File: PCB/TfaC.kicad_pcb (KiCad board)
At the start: 2 copper layers, 105 x 54 mm, 52 parts, among them IC501 ATMEGA88-A, M301 DisplayModule, P101 Line, P501 PRG, Q401 IRLML2502, Q402 IRLML2502, Q403 IRLML2502, Q404 IRLML2502, Q405 IRLML2502, Q406 IRLML2502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

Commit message: Touched up some routs to avoid zone borders
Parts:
- moved G*** 7.87 mm to (180.2, 68.1)
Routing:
- net /Controller/~RTC_SELECT: track 80.3 -> 119.6 mm
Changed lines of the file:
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@@
     (thickness 1.6)
     (drawings 64)
-    (tracks 431)
+    (tracks 435)
     (zones 0)
     (modules 52)
@@
   )
   (setup
-    (last_trace_width 0.1524)
+    (last_trace_width 0.3048)
     (user_trace_width 0.3048)
     (user_trace_width 0.6096)
@@
   )
   (module tfac-footprints:sm-logo-1200 (layer F.Cu)
-    (at 188.087 68.072)
+    (at 180.213 68.072)
     (fp_text reference G*** (at 0 0) (layer F.SilkS) hide
       (effects (font (thickness 0.3)))
@@
   (segment (start 148.148 85.41) (end 148.148 87.242) (width 0.6096) (layer F.Cu) (net 15))
   (segment (start 147.24 84.502) (end 148.148 85.41) (width 0.6096) (layer F.Cu) (net 15))
-  (segment (start 136.38022 101.092) (end 136.38022 98.69678) (width 0.3048) (layer F.Cu) (net 16))
-  (segment (start 181.362 83.306) (end 181.362 82.618) (width 0.3048) (layer F.Cu) (net 16))
-  (segment (start 180.721 83.947) (end 181.362 83.306) (width 0.3048) (layer F.Cu) (net 16))
-  (segment (start 180.721 84.201) (end 180.721 83.947) (width 0.3048) (layer F.Cu) (net 16))
-  (segment (start 180.594 84.328) (end 180.721 84.201) (width 0.3048) (layer F.Cu) (net 16))
-  (via (at 180.594 84.328) (size 0.6858) (drill 0.3302) (layers F.Cu B.Cu) (net 16))
-  (segment (start 179.324 85.598) (end 180.594 84.328) (width 0.3048) (layer B.Cu) (net 16))
-  (segment (start 170.561 85.598) (end 179.324 85.598) (width 0.3048) (layer B.Cu) (net 16))
-  (segment (start 159.131 97.028) (end 170.561 85.598) (width 0.3048) (layer B.Cu) (net 16))
-  (segment (start 140.335 97.028) (end 159.131 97.028) (width 0.3048) (layer B.Cu) (net 16))
-  (segment (start 140.081 96.774) (end 140.335 97.028) (width 0.3048) (layer B.Cu) (net 16))
-  (via (at 140.081 96.774) (size 0.6858) (drill 0.3302) (layers F.Cu B.Cu) (net 16))
-  (segment (start 138.303 96.774) (end 140.081 96.774) (width 0.3048) (layer F.Cu) (net 16))
-  (segment (start 136.38022 98.69678) (end 138.303 96.774) (width 0.3048) (layer F.Cu) (net 16))
+  (segment (start 138.684 102.188) (end 138.684 103.759) (width 0.3048) (layer F.Cu) (net 16) (status 400000))
+  (segment (start 180.721 83.82) (end 181.362 83.179) (width 0.3048) (layer F.Cu) (net 16) (status 800000))
+  (segment (start 180.721 84.201) (end 180.721 83.82) (width 0.3048) (layer F.Cu) (net 16))
+  (segment (start 180.34 84.582) (end 180.721 84.201) (width 0.3048) (layer F.Cu) (net 16))
+  (via (at 180.34 84.582) (size 0.6858) (drill 0.3302) (layers F.Cu B.Cu) (net 16))
+  (segment (start 179.705 85.217) (end 180.34 84.582) (width 0.3048) (layer B.Cu) (net 16))
+  (segment (start 173.355 85.217) (end 179.705 85.217) (width 0.3048) (layer B.Cu) (net 16))
+  (segment (start 153.543 105.029) (end 173.355 85.217) (width 0.3048) (layer B.Cu) (net 16))
+  (segment (start 139.954 105.029) (end 153.543 105.029) (width 0.3048) (layer B.Cu) (net 16))
+  (segment (start 139.827 104.902) (end 139.954 105.029) (width 0.3048) (layer B.Cu) (net 16))
+  (via (at 139.827 104.902) (size 0.6858) (drill 0.3302) (layers F.Cu B.Cu) (net 16))
+  (segment (start 138.684 103.759) (end 139.827 104.902) (width 0.3048) (layer F.Cu) (net 16))
+  (segment (start 181.362 83.179) (end 181.362 82.618) (width 0.3048) (layer F.Cu) (net 16) (status C00000))
   (segment (start 136.38022 101.092) (end 137.588 101.092) (width 0.6096) (layer F.Cu) (net 16))
   (segment (start 137.588 101.092) (end 138.684 102.188) (width 0.6096) (layer F.Cu) (net 16))
@@
   (segment (start 136.38022 86.36) (end 137.588 86.36) (width 0.6096) (layer F.Cu) (net 17))
   (segment (start 137.588 86.36) (end 138.938 87.71) (width 0.6096) (layer F.Cu) (net 17))
+  (segment (start 119.634 86.741) (end 119.634 102.108) (width 0.3048) (layer B.Cu) (net 18))
   (segment (start 117.87378 79.0448) (end 117.87378 81.55178) (width 0.3048) (layer F.Cu) (net 18))
+  (segment (start 119.634 83.312) (end 119.634 86.741) (width 0.3048) (layer B.Cu) (net 18))
+  (segment (start 118.618 82.296) (end 119.634 83.312) (width 0.3048) (layer B.Cu) (net 18))
+  (via (at 118.618 82.296) (size 0.6858) (drill 0.3302) (layers F.Cu B.Cu) (net 18))
+  (segment (start 117.87378 81.55178) (end 118.618 82.296) (width 0.3048) (layer F.Cu) (net 18))
+  (segment (start 171.196 101.854) (end 175.514 97.536) (width 0.3048) (layer B.Cu) (net 18))
+  (segment (start 171.196 108.331) (end 171.196 101.854) (width 0.3048) (layer B.Cu) (net 18))
+  (segment (start 162.306 117.221) (end 171.196 108.331) (width 0.3048) (layer B.Cu) (net 18))
+  (segment (start 120.65 117.221) (end 162.306 117.221) (width 0.3048) (layer B.Cu) (net 18))
+  (segment (start 117.856 114.427) (end 120.65 117.221) (width 0.3048) (layer B.Cu) (net 18))
+  (segment (start 117.856 103.886) (end 117.856 114.427) (width 0.3048) (layer B.Cu) (net 18))
+  (segment (start 119.634 102.108) (end 117.856 103.886) (width 0.3048) (layer B.Cu) (net 18))
+  (segment (start 174.752 98.298) (end 175.514 97.536) (width 0.3048) (layer B.Cu) (net 18))
   (segment (start 178.962 92.564) (end 178.962 91.118) (width 0.3048) (layer F.Cu) (net 18))
   (segment (start 178.943 92.583) (end 178.962 92.564) (width 0.3048) (layer F.Cu) (net 18))
   (via (at 178.943 92.583) (size 0.6858) (drill 0.3302) (layers F.Cu B.Cu) (net 18))
   (segment (start 178.943 94.107) (end 178.943 92.583) (width 0.3048) (layer B.Cu) (net 18))
-  (segment (start 174.752 98.298) (end 178.943 94.107) (width 0.3048) (layer B.Cu) (net 18))
-  (segment (start 167.64 98.298) (end 174.752 98.298) (width 0.3048) (layer B.Cu) (net 18))
-  (segment (start 167.005 97.663) (end 167.64 98.298) (width 0.3048) (layer B.Cu) (net 18))
-  (segment (start 130.556 97.663) (end 167.005 97.663) (width 0.3048) (layer B.Cu) (net 18))
-  (segment (start 119.634 86.741) (end 130.556 97.663) (width 0.3048) (layer B.Cu) (net 18))
-  (segment (start 119.634 83.312) (end 119.634 86.741) (width 0.3048) (layer B.Cu) (net 18))
-  (segment (start 118.618 82.296) (end 119.634 83.312) (width 0.3048) (layer B.Cu) (net 18))
-  (via (at 118.618 82.296) (size 0.6858) (drill 0.3302) (layers F.Cu B.Cu) (net 18))
-  (segment (start 117.87378 81.55178) (end 118.618 82.296) (width 0.3048) (layer F.Cu) (net 18))
+  (segment (start 175.514 97.536) (end 178.943 94.107) (width 0.3048) (layer B.Cu) (net 18))
   (segment (start 115.4176 77.644) (end 116.47298 77.644) (width 0.6096) (layer F.Cu) (net 18))
   (segment (start 116.47298 77.644) (end 117.87378 79.0448) (width 0.6096) (layer F.Cu) (net 18))

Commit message: Created gerbers for TfaC-Rev 2L.2.a2f0245
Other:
- board text added: "TfaC Rev 2L.2.a2f0245"
- board text removed: "TfaC Rev 2L.2"
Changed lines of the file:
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@@
   )
   (setup
-    (last_trace_width 0.3048)
+    (last_trace_width 0.1524)
     (user_trace_width 0.3048)
     (user_trace_width 0.6096)
@@
     (effects (font (size 0.762 0.762) (thickness 0.127)))
   )
-  (gr_text "TfaC\nRev 2L.2\n" (at 200.5584 68.3768) (layer F.SilkS)
+  (gr_text "TfaC\nRev 2L.2.a2f0245\n" (at 200.5584 68.3768) (layer F.SilkS)
     (effects (font (size 1.27 1.27) (thickness 0.127)) (justify right))
   )
@@
   (segment (start 148.148 85.41) (end 148.148 87.242) (width 0.6096) (layer F.Cu) (net 15))
   (segment (start 147.24 84.502) (end 148.148 85.41) (width 0.6096) (layer F.Cu) (net 15))
-  (segment (start 138.684 102.188) (end 138.684 103.759) (width 0.3048) (layer F.Cu) (net 16) (status 400000))
-  (segment (start 180.721 83.82) (end 181.362 83.179) (width 0.3048) (layer F.Cu) (net 16) (status 800000))
+  (segment (start 138.684 102.188) (end 138.684 103.759) (width 0.3048) (layer F.Cu) (net 16))
+  (segment (start 180.721 83.82) (end 181.362 83.179) (width 0.3048) (layer F.Cu) (net 16))
   (segment (start 180.721 84.201) (end 180.721 83.82) (width 0.3048) (layer F.Cu) (net 16))
   (segment (start 180.34 84.582) (end 180.721 84.201) (width 0.3048) (layer F.Cu) (net 16))
@@
   (via (at 139.827 104.902) (size 0.6858) (drill 0.3302) (layers F.Cu B.Cu) (net 16))
   (segment (start 138.684 103.759) (end 139.827 104.902) (width 0.3048) (layer F.Cu) (net 16))
-  (segment (start 181.362 83.179) (end 181.362 82.618) (width 0.3048) (layer F.Cu) (net 16) (status C00000))
+  (segment (start 181.362 83.179) (end 181.362 82.618) (width 0.3048) (layer F.Cu) (net 16))
   (segment (start 136.38022 101.092) (end 137.588 101.092) (width 0.6096) (layer F.Cu) (net 16))
   (segment (start 137.588 101.092) (end 138.684 102.188) (width 0.6096) (layer F.Cu) (net 16))

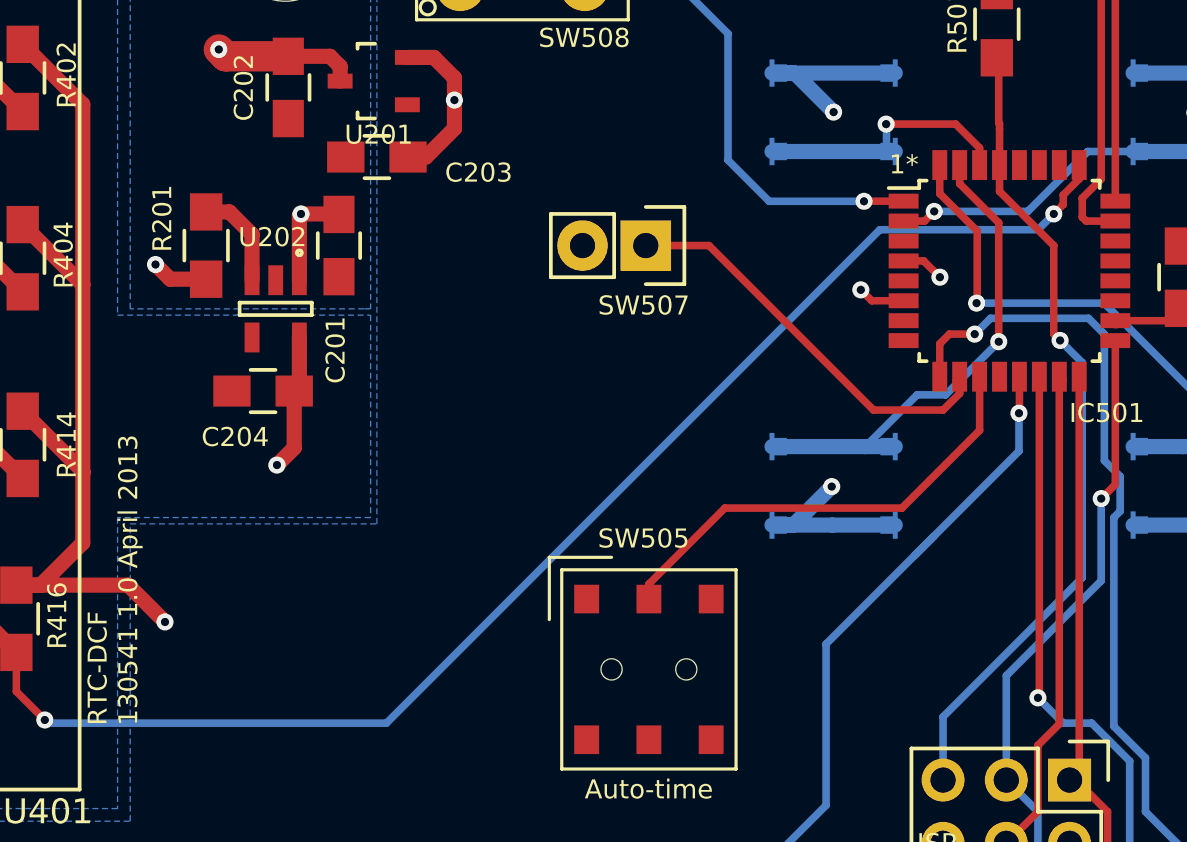
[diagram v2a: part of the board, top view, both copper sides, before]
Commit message: Added indicator LEDs and Heartbeat
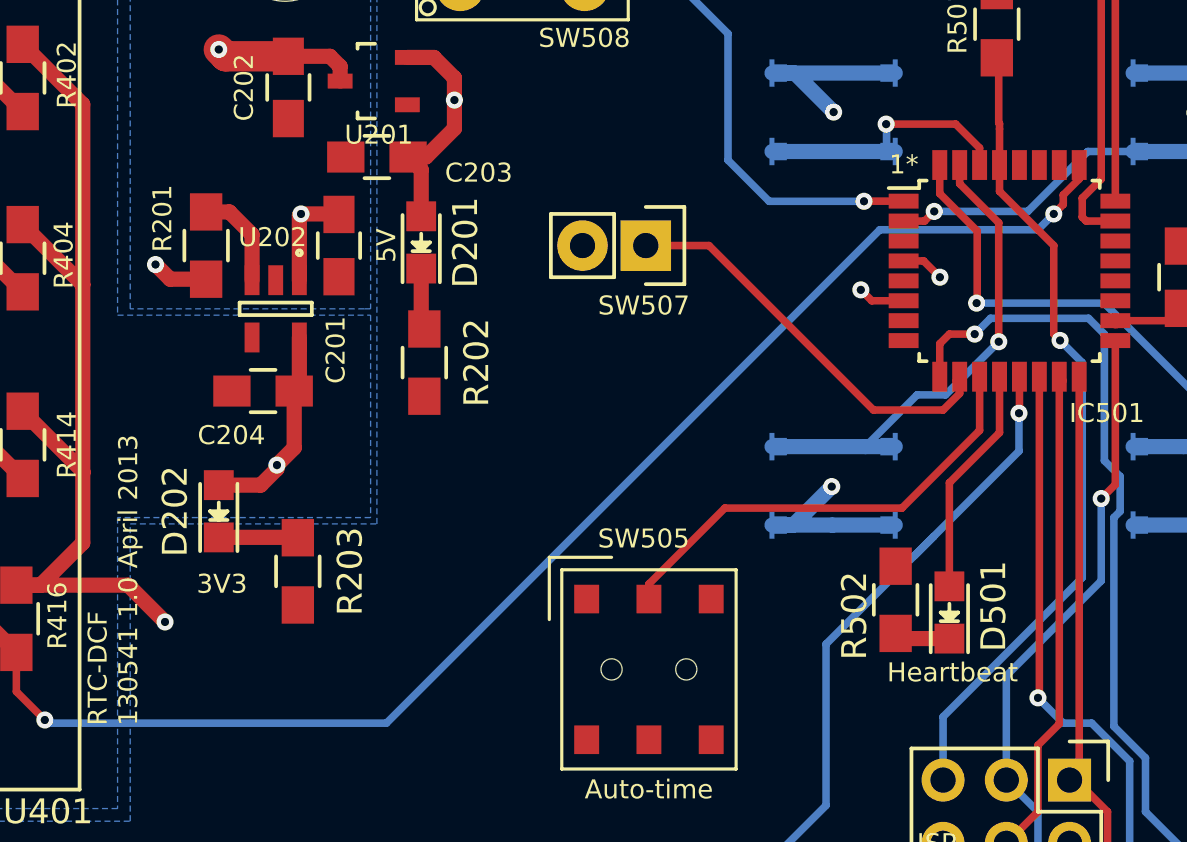
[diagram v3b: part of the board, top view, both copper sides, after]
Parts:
- added D201: LED, LEDs:LED-0805, F.Cu at (154.9, 85.7)
- added D202: LED, LEDs:LED-0805, F.Cu at (146.8, 96.5)
- added D501: LED, LEDs:LED-0805, F.Cu at (176.1, 100.6)
- added R202: 480Ω, Resistors_SMD:R_0805_HandSoldering, F.Cu at (155.1, 90.6)
- added R203: 260Ω, Resistors_SMD:R_0805_HandSoldering, F.Cu at (150.0, 98.9)
- added R502: 480Ω, Resistors_SMD:R_0805_HandSoldering, F.Cu at (174.0, 100.1)
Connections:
- IC501 pad 12: Net-(IC501-Pad12) -> /Controller/Heartbeat
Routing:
- net /Controller/Heartbeat: track 0.00 -> 9.25 mm
- net Net-(D202-Pad1): track 0.00 -> 3.18 mm
- net /Power System/Vbb: track 43.8 -> 46.6 mm
- net /Controller/Vcc: track 100.2 -> 102.9 mm
- net Net-(D201-Pad1): track 0.00 -> 2.48 mm
- net Net-(D501-Pad1): track 0.00 -> 2.24 mm
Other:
- board text added: "3V3"
- board text added: "5V"
- board text added: "Heartbeat"

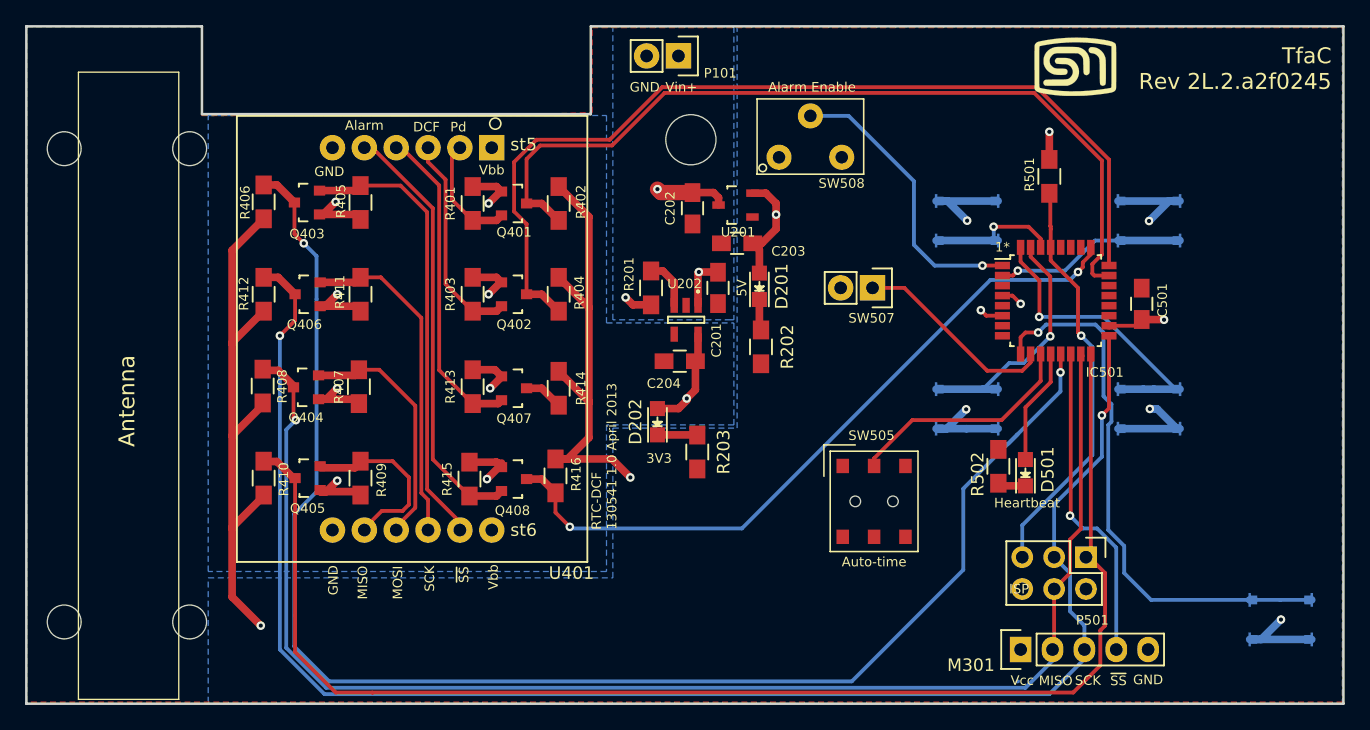
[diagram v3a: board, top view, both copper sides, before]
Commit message: Updated the board for further features to the display
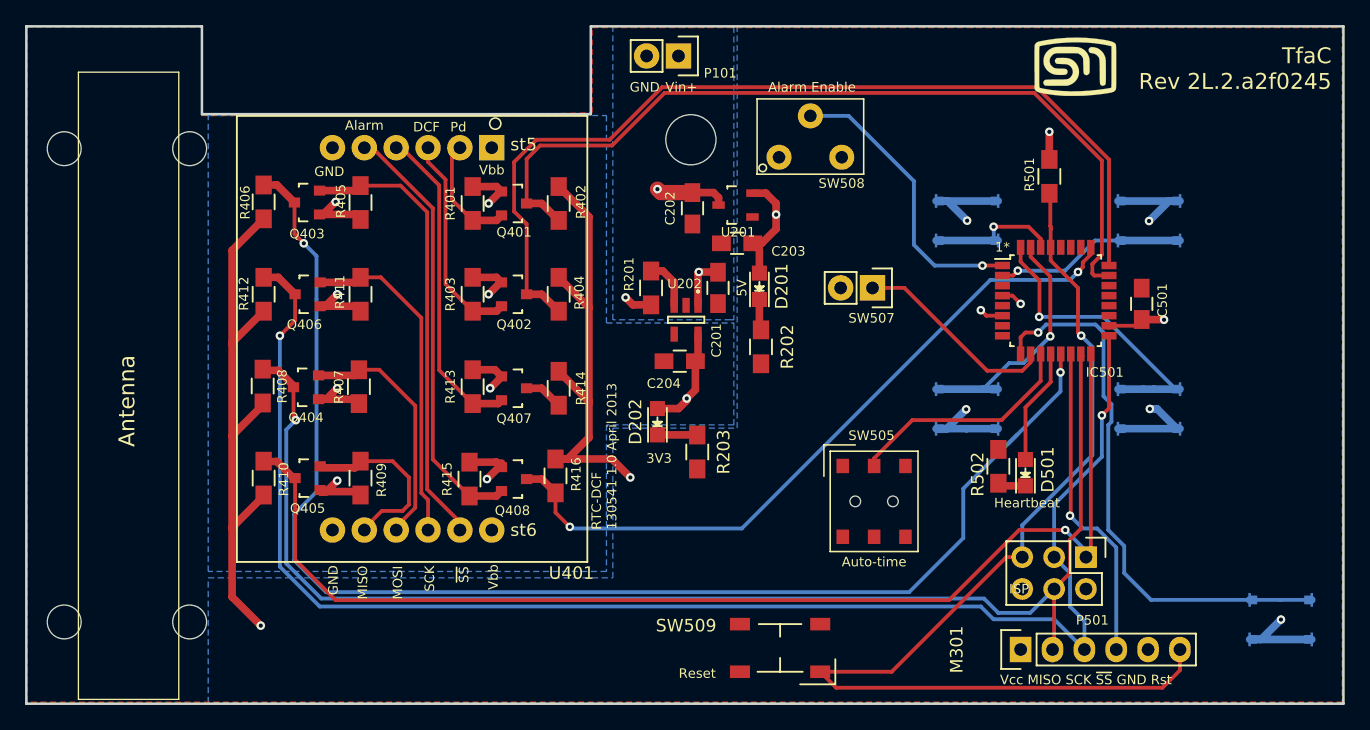
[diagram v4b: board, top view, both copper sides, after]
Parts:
- added SW509: Reset, tfac-footprints:PTS525SM15SMTR2LFS, F.Cu at (156.6, 114.6)
- M301: footprint Pin_Headers:Pin_Header_Straight_1x05 -> Pin_Headers:Pin_Header_Straight_1x06
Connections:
- IC501 pad 29: Reset -> /Controller/Reset
- P501 pad 5: Reset -> /Controller/Reset
- R501 pad 2: Reset -> /Controller/Reset
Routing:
- net /Controller/Reset: track 0.00 -> 84.8 mm, vias 0 -> 1
- net Reset: track 33.9 -> 0.00 mm, vias 1 -> 0
- net /Controller/MISO: track 109.7 -> 94.4 mm, vias 0 -> 1
- net /Controller/~RTC_SELECT: track 119.6 -> 108.2 mm
- net /Controller/SCK: track 128.4 -> 121.1 mm
- net /Controller/MOSI: track 113.4 -> 107.2 mm
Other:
- board text added: "Reset"
- board text added: "Vcc MISO SCK ~SS~ GND Rst"
- board text removed: "Vcc"

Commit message: Updated revision number
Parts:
- moved G*** 7.62 mm to (187.8, 67.9)
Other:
- board text added: "TfaC Rev 2L.3"
- board text removed: "TfaC Rev 2L.2.a2f0245"
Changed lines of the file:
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@@
     (links 152)
     (no_connects 0)
-    (area 96.399999 64.899999 201.600001 119.100001)
+    (area 94.440438 63.8107 201.600001 120.920762)
     (thickness 1.6)
     (drawings 64)
@@
   )
   (setup
-    (last_trace_width 0.3048)
+    (last_trace_width 0.1524)
     (user_trace_width 0.3048)
     (user_trace_width 0.6096)
@@
   )
   (module tfac-footprints:sm-logo-1200 (layer F.Cu)
-    (at 180.213 68.072)
+    (at 187.833 67.945)
     (fp_text reference G*** (at 0 0) (layer F.SilkS) hide
       (effects (font (thickness 0.3)))
@@
     (effects (font (size 0.762 0.762) (thickness 0.127)))
   )
-  (gr_text "TfaC\nRev 2L.2.a2f0245\n" (at 200.5584 68.3768) (layer F.SilkS)
+  (gr_text "TfaC\nRev 2L.3\n" (at 200.5584 68.3768) (layer F.SilkS)
     (effects (font (size 1.27 1.27) (thickness 0.127)) (justify right))
   )

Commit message: Corrected the symbol and footprint for the reset switch
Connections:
- IC501 pad 19: Net-(IC501-Pad19) -> (no net)
- IC501 pad 20: Net-(IC501-Pad20) -> (no net)
- IC501 pad 22: Net-(IC501-Pad22) -> (no net)
- IC501 pad 26: Net-(IC501-Pad26) -> (no net)
- IC501 pad 27: Net-(IC501-Pad27) -> (no net)
- IC501 pad 28: Net-(IC501-Pad28) -> (no net)
- IC501 pad 7: Net-(IC501-Pad7) -> (no net)
- IC501 pad 8: Net-(IC501-Pad8) -> (no net)
- SW505 pad 1: Net-(SW505-Pad1) -> (no net)
- SW508 pad 1: Net-(SW508-Pad1) -> (no net)
- SW509 pad 2: GND -> /Controller/Reset
- SW509 pad 3: (no net) -> GND
- SW509 pad 4: (no net) -> GND
- U202 pad 4: Net-(U202-Pad4) -> (no net)
